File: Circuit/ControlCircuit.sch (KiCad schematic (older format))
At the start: 16 parts, among them P101 CONN_01X08, P102 CONN_01X08, P103 CONN_01X08, P104 CONN_01X08, P105 CONN_01X08, P106 CONN_01X08, P107 CONN_01X02

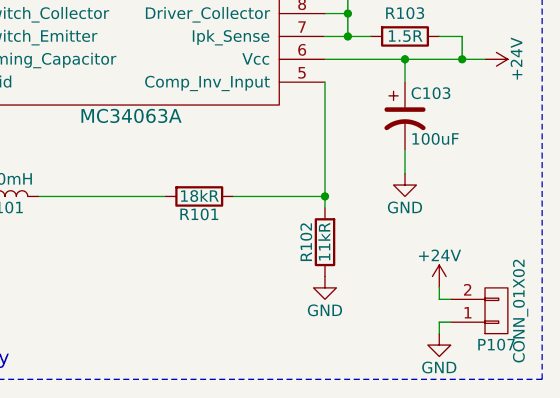
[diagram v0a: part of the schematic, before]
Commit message: PCB rev 1 ordered. Components counted
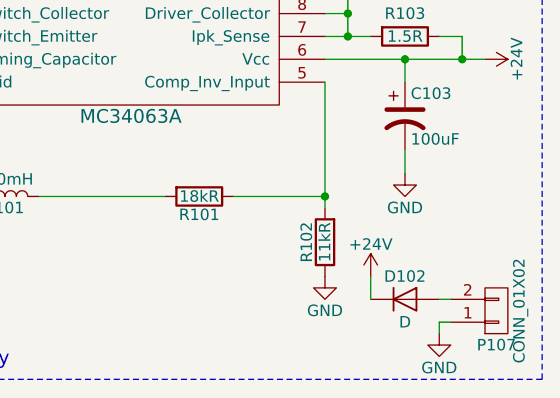
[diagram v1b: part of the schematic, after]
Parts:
- added D102: D, Diodes_SMD:D_MELF_Standard, symbol D
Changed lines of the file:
@@
 L +24V #PWR010
 U 1 1 58B0861D
-P 10450 5500
-F 0 "#PWR010" H 10450 5350 50  0001 C CNN
-F 1 "+24V" H 10450 5640 50  0000 C CNN
-F 2 "" H 10450 5500 50  0000 C CNN
-F 3 "" H 10450 5500 50  0000 C CNN
-	1    10450 5500
+P 10150 5450
+F 0 "#PWR010" H 10150 5300 50  0001 C CNN
+F 1 "+24V" H 10150 5590 50  0000 C CNN
+F 2 "" H 10150 5450 50  0000 C CNN
+F 3 "" H 10150 5450 50  0000 C CNN
+	1    10150 5450
 	1    0    0    -1
 $EndComp
@@
 	10450 5650 10500 5650
 Wire Wire Line
-	10450 5500 10450 5550
-Wire Wire Line
-	10450 5550 10500 5550
-Wire Wire Line
 	1850 3900 2250 3900
 Wire Wire Line
@@
 	1    0    0    -1
 $EndComp
+$Comp
+L D D102
+U 1 1 58BAFEB2
+P 10300 5550
+F 0 "D102" H 10300 5650 50  0000 C CNN
+F 1 "D" H 10300 5450 50  0000 C CNN
+F 2 "Diodes_SMD:D_MELF_Standard" H 10300 5550 50  0001 C CNN
+F 3 "" H 10300 5550 50  0000 C CNN
+	1    10300 5550
+	1    0    0    -1
+$EndComp
+Wire Wire Line
+	10150 5450 10150 5550
+Wire Wire Line
+	10450 5550 10500 5550
 $EndSCHEMATC

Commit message: Report writing
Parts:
- C101: footprint Capacitors_SMD:C_0805 -> Capacitors_SMD:C_1206
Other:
- moved on the sheet: L101
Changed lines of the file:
@@
 L L L101
 U 1 1 58ADC41A
-P 8550 5100
-F 0 "L101" V 8500 5100 50  0000 C CNN
-F 1 "260mH" V 8625 5100 50  0000 C CNN
-F 2 "Inductors:Inductor_Wurth_HCI-7050" H 8550 5100 50  0001 C CNN
-F 3 "" H 8550 5100 50  0000 C CNN
-	1    8550 5100
-	0    -1   -1   0
+P 7700 4750
+F 0 "L101" V 7750 4750 50  0000 C CNN
+F 1 "260mH" V 7850 4750 50  0000 C CNN
+F 2 "Inductors:Inductor_Wurth_HCI-7050" H 7700 4750 50  0001 C CNN
+F 3 "" H 7700 4750 50  0000 C CNN
+	1    7700 4750
+	-1   0    0    1
 $EndComp
 $Comp
@@
 F 0 "C101" H 7725 5400 50  0000 L CNN
 F 1 "4uF" H 7725 5200 50  0000 L CNN
-F 2 "Capacitors_SMD:C_0805" H 7700 5300 50  0001 C CNN
+F 2 "Capacitors_SMD:C_1206" H 7700 5300 50  0001 C CNN
 F 3 "" H 7700 5300 50  0000 C CNN
 	1    7700 5300
@@
 Wire Wire Line
 	7950 4500 8200 4500
-Wire Wire Line
-	7700 4400 7700 5150
 Connection ~ 7700 4400
 Wire Wire Line
-	7450 5100 8400 5100
+	7450 5100 9250 5100
 Connection ~ 7700 5100
-Wire Wire Line
-	8700 5100 9250 5100
 Wire Wire Line
 	9550 5100 9950 5100
@@
 Wire Wire Line
 	10450 5550 10500 5550
+Wire Wire Line
+	7700 4600 7700 4400
+Wire Wire Line
+	7700 4900 7700 5150
 $EndSCHEMATC
